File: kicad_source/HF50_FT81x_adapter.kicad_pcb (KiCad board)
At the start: 2 copper layers, 30 x 31 mm, 2 parts, among them P1 CONN_01X09, P2 CONN_01X08

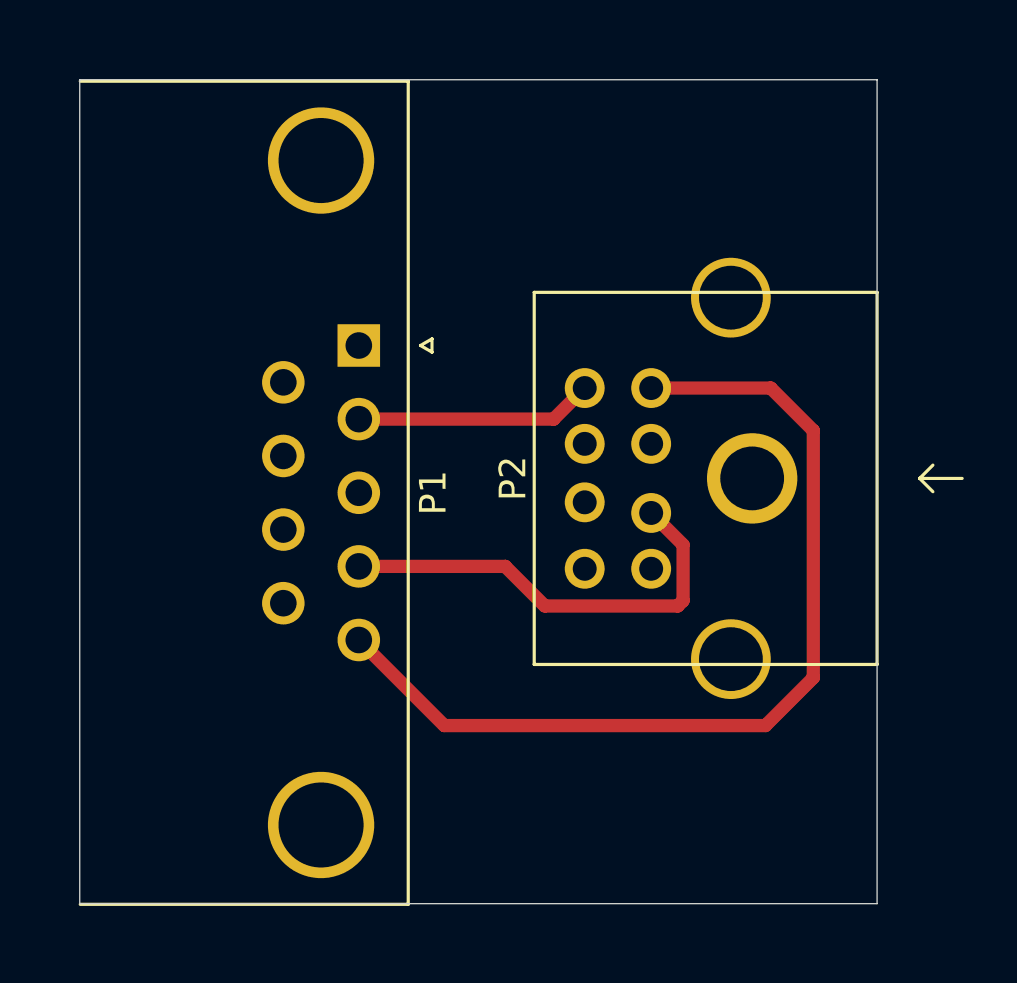
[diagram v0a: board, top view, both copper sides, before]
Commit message: added LED
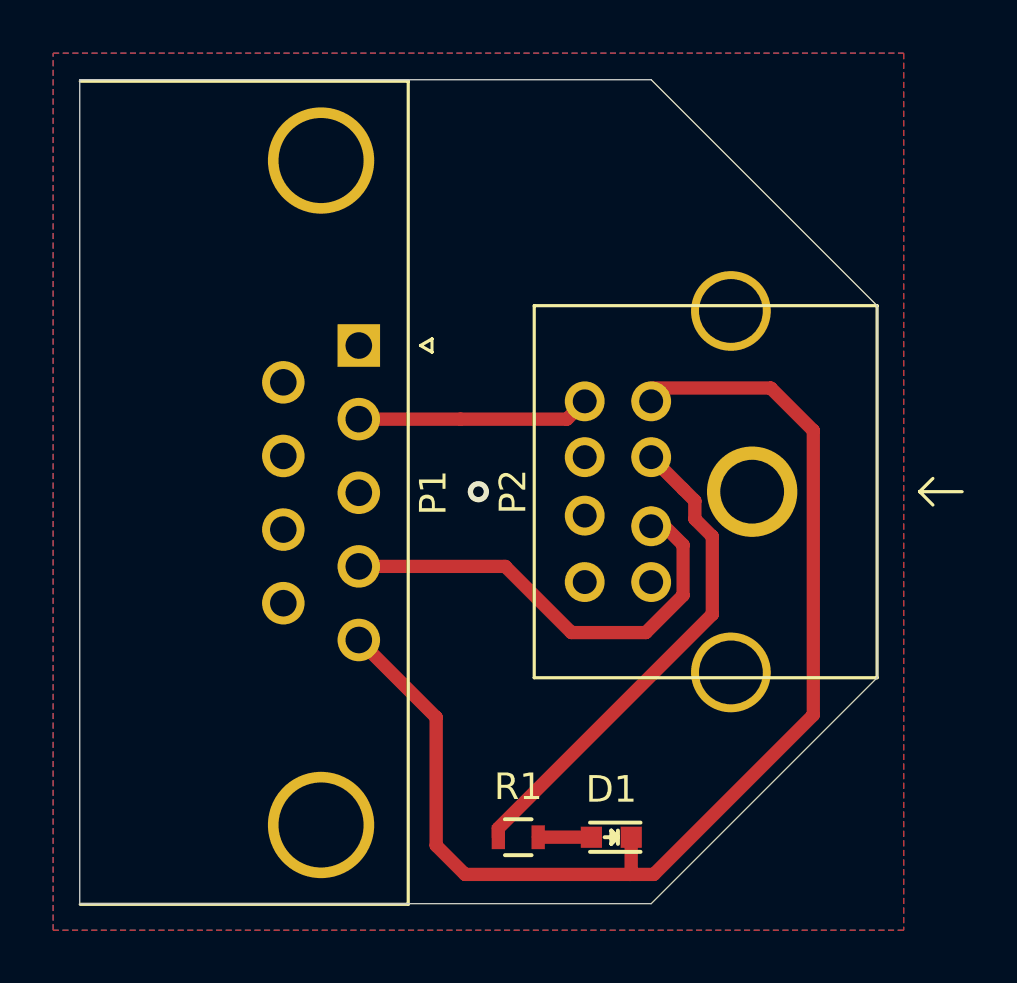
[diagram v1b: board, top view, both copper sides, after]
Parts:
- added D1: 150060GS75000, LEDs:LED_0603, F.Cu at (106.0, 139.5)
- added R1: 10k, resistors:R_0603, F.Cu at (102.5, 139.5)
- P2: value CONN_01X08 -> KMDGX-8S-BS
- moved P2 0.50 mm to (116.0, 126.5)
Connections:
- P2 pad 1: (no net) -> /+13.8V
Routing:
- net /+13.8V: track 0.00 -> 18.6 mm
- net GND: track 35.2 -> 44.9 mm, vias 0 -> 1
- net Net-(D1-Pad2): track 0.00 -> 2.00 mm
- net /PTT: track 16.7 -> 17.4 mm
- added copper zone on B.Cu, net GND
- added copper zone on F.Cu, net GND
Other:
- outline, holes or cut-outs redrawn

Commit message: added mounting holes
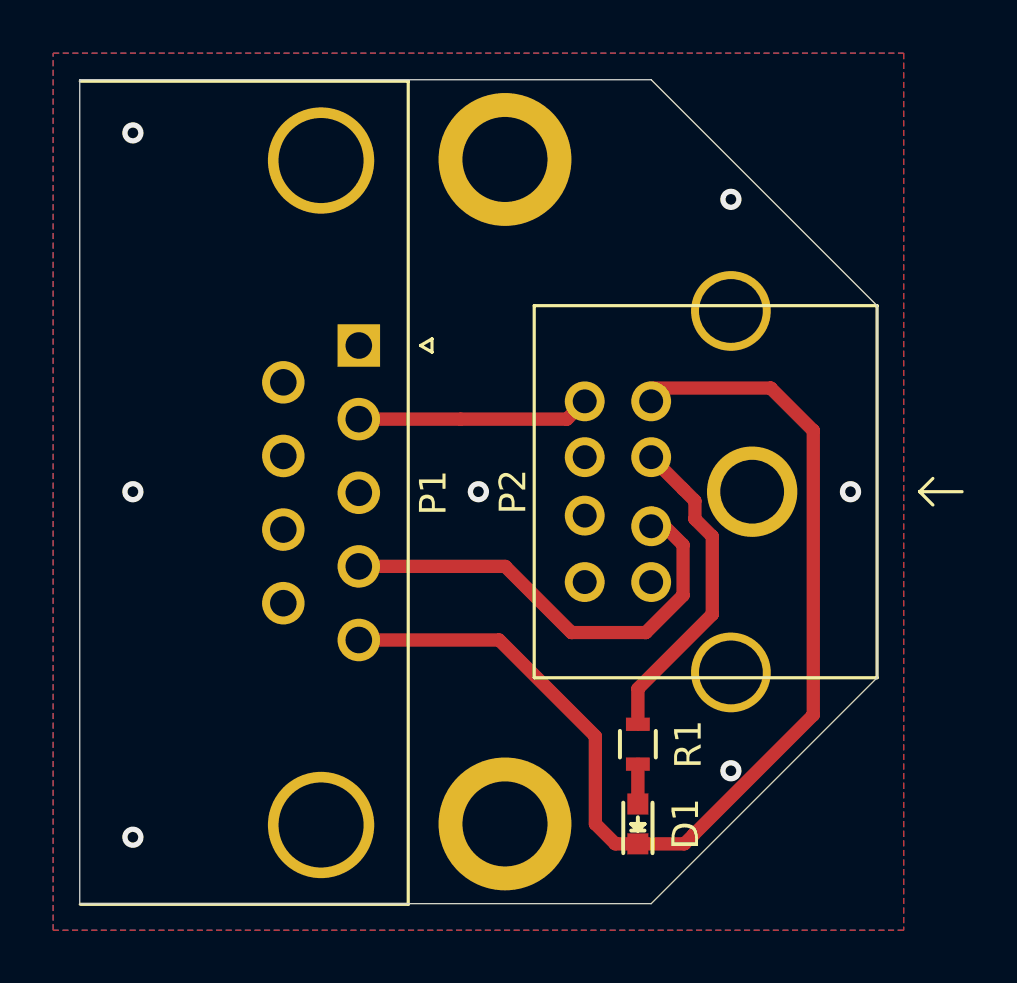
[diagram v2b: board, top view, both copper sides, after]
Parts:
- added MECH1: MHP_3.2_5.0, MECH_mounting_holes:MHP_3.2_5.0, F.Cu at (102.0, 114.0)
- added MECH2: MHP_3.2_5.0, MECH_mounting_holes:MHP_3.2_5.0, F.Cu at (102.0, 139.0)
- moved R1 5.70 mm to (107.0, 136.0), turned to 270 degrees
- moved D1 1.12 mm to (107.0, 139.0), turned to 90 degrees
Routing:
- net /+13.8V: track 18.6 -> 12.2 mm
- net GND: track 44.9 -> 41.7 mm, vias 1 -> 7
- net Net-(D1-Pad2): track 2.00 -> 1.50 mm
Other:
- board text added: "Adapter by OE5LXR & DL1MAB"
- board text added: "Yeasu FT81x ACC"
- board text added: "connect Hardrock 50 on this side"

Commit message: updated BOM and images, added link to aisler
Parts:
- P1: value CONN_01X09 -> LD09P33E4GX00LF

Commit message: updated to Kicad 6
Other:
- net class Default removed

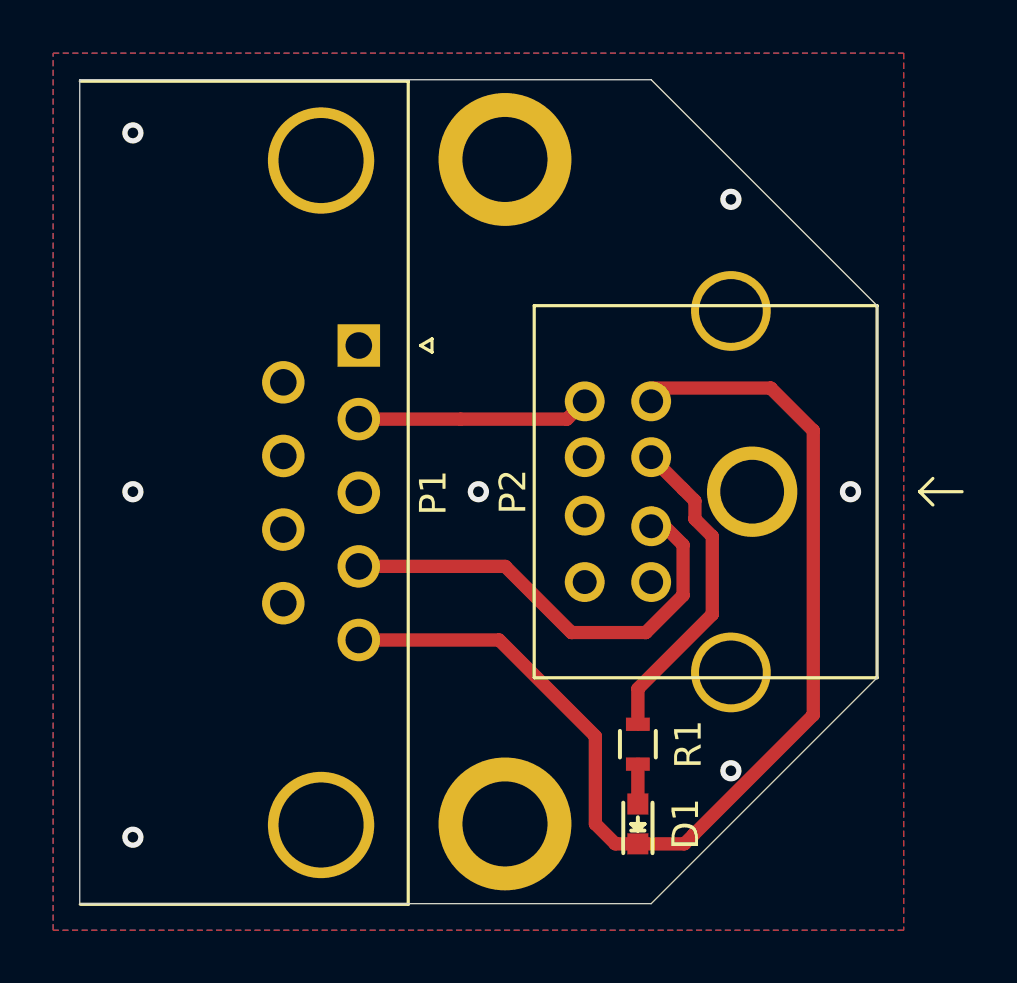
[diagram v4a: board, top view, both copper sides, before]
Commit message: switched to THT parts
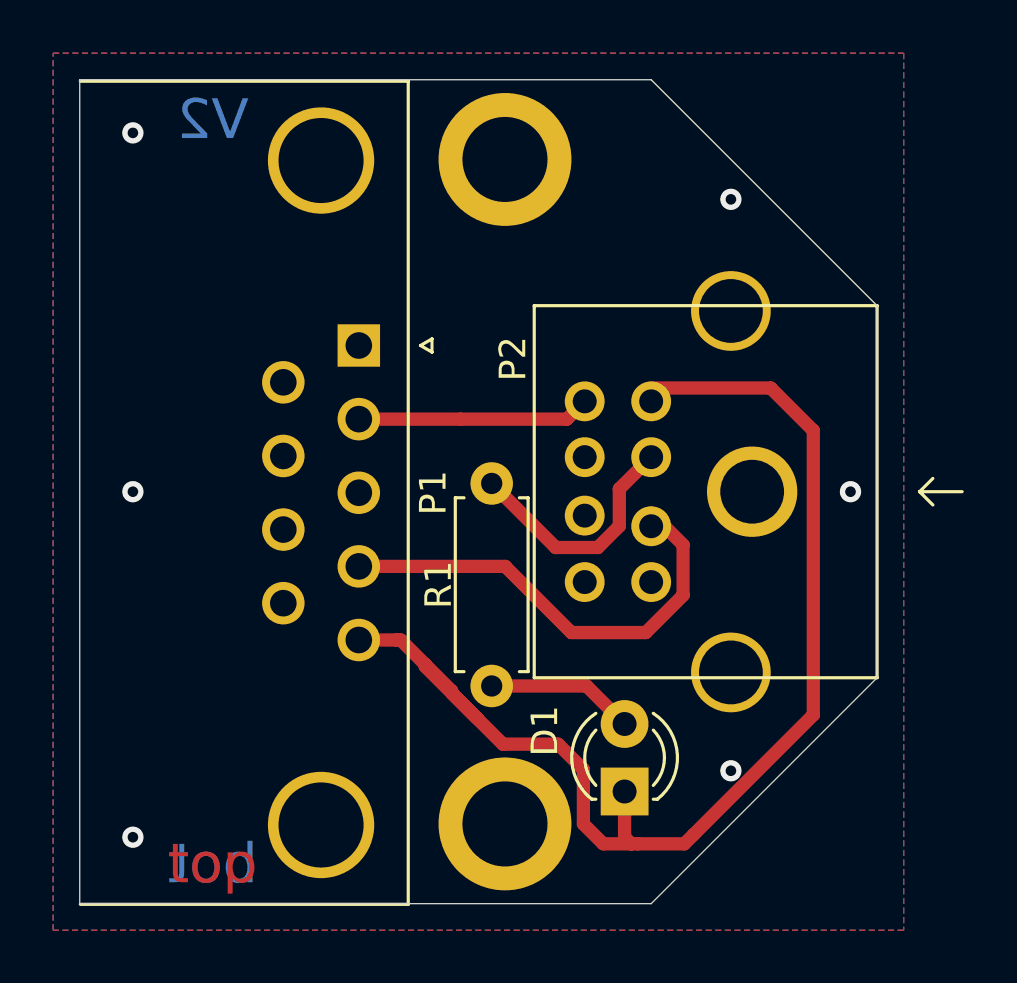
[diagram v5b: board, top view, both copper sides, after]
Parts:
- D1: footprint LEDs:LED_0603 -> LED_THT:LED_D3.0mm
- R1: footprint resistors:R_0603 -> Resistor_THT:R_Axial_DIN0207_L6.3mm_D2.5mm_P7.62mm_Horizontal
- moved R1 11.2 mm to (101.5, 126.2)
- moved D1 1.32 mm to (106.5, 137.8)
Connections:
- MECH1 pad 1: (no net) -> unconnected-(MECH1-Pad1)
- MECH2 pad 1: (no net) -> unconnected-(MECH2-Pad1)
- P1 pad 1: (no net) -> unconnected-(P1-Pad1)
- P1 pad 3: (no net) -> unconnected-(P1-Pad3)
- P1 pad 6: (no net) -> unconnected-(P1-Pad6)
- P1 pad 7: (no net) -> unconnected-(P1-Pad7)
- P1 pad 8: (no net) -> unconnected-(P1-Pad8)
- P1 pad 9: (no net) -> unconnected-(P1-Pad9)
- P2 pad 4: (no net) -> unconnected-(P2-Pad4)
- P2 pad 5: (no net) -> unconnected-(P2-Pad5)
- P2 pad 7: (no net) -> unconnected-(P2-Pad7)
- P2 pad 8: (no net) -> unconnected-(P2-Pad8)
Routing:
- net GND: track 41.7 -> 45.9 mm, vias 7 -> 6
- net Net-(D1-Pad2): track 1.50 -> 5.59 mm
- net /+13.8V: track 12.2 -> 9.22 mm
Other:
- board text added: "V2"
- board text added: "bot"
- board text added: "top"
